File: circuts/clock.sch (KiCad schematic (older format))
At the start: 20 parts, among them P1 IN, P2 OUT, P3 LED OUTPUT, P4 PWR 12v, Q1 2N7002, Q2 2N7002, Q3 2N7002, Q4 2N7002, Q5 2N7002, Q6 2N7002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

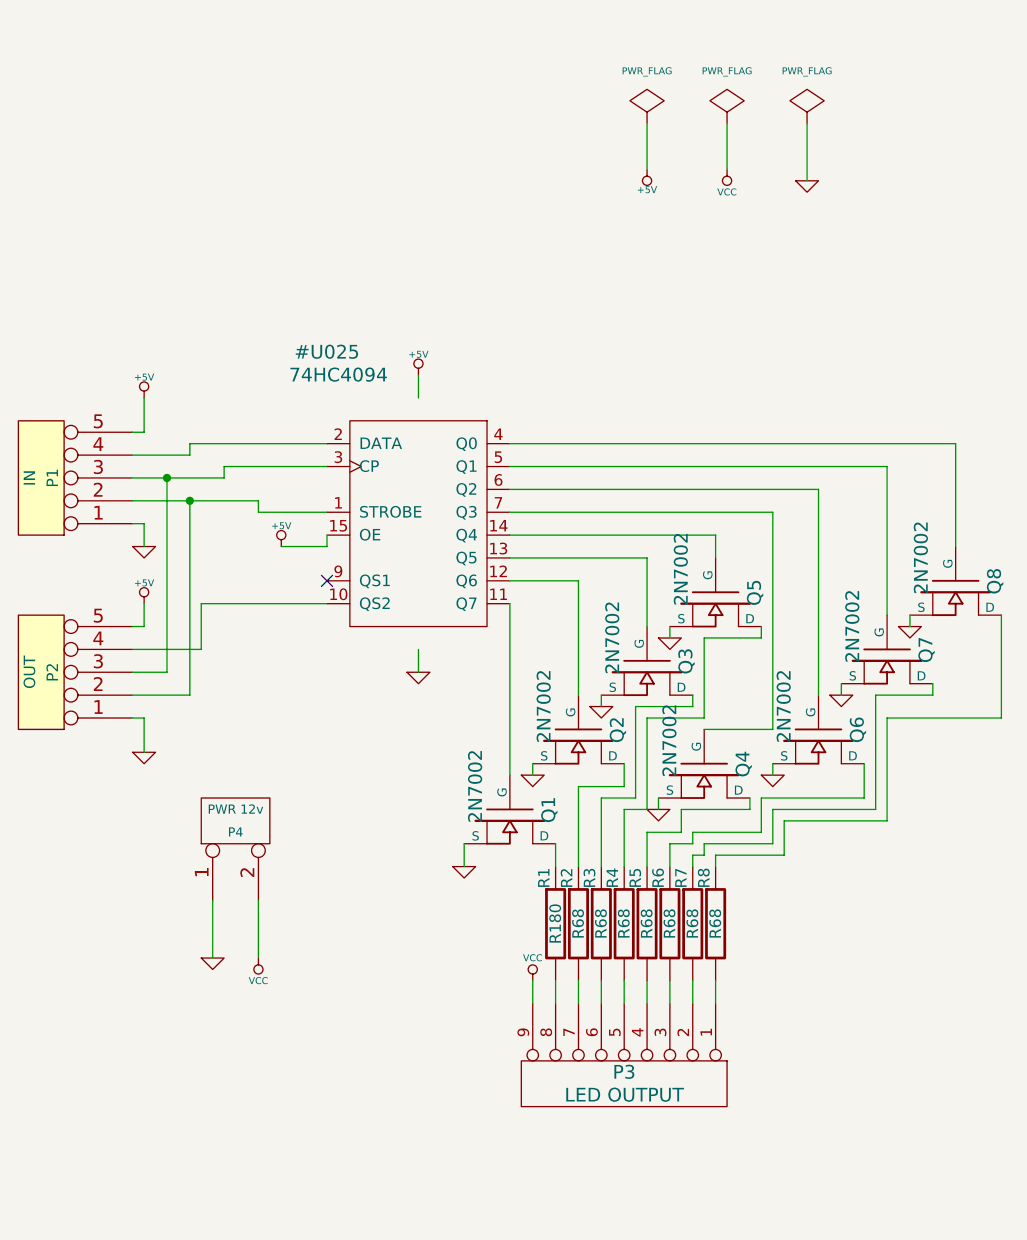
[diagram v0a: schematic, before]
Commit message: Release of circut for LED output
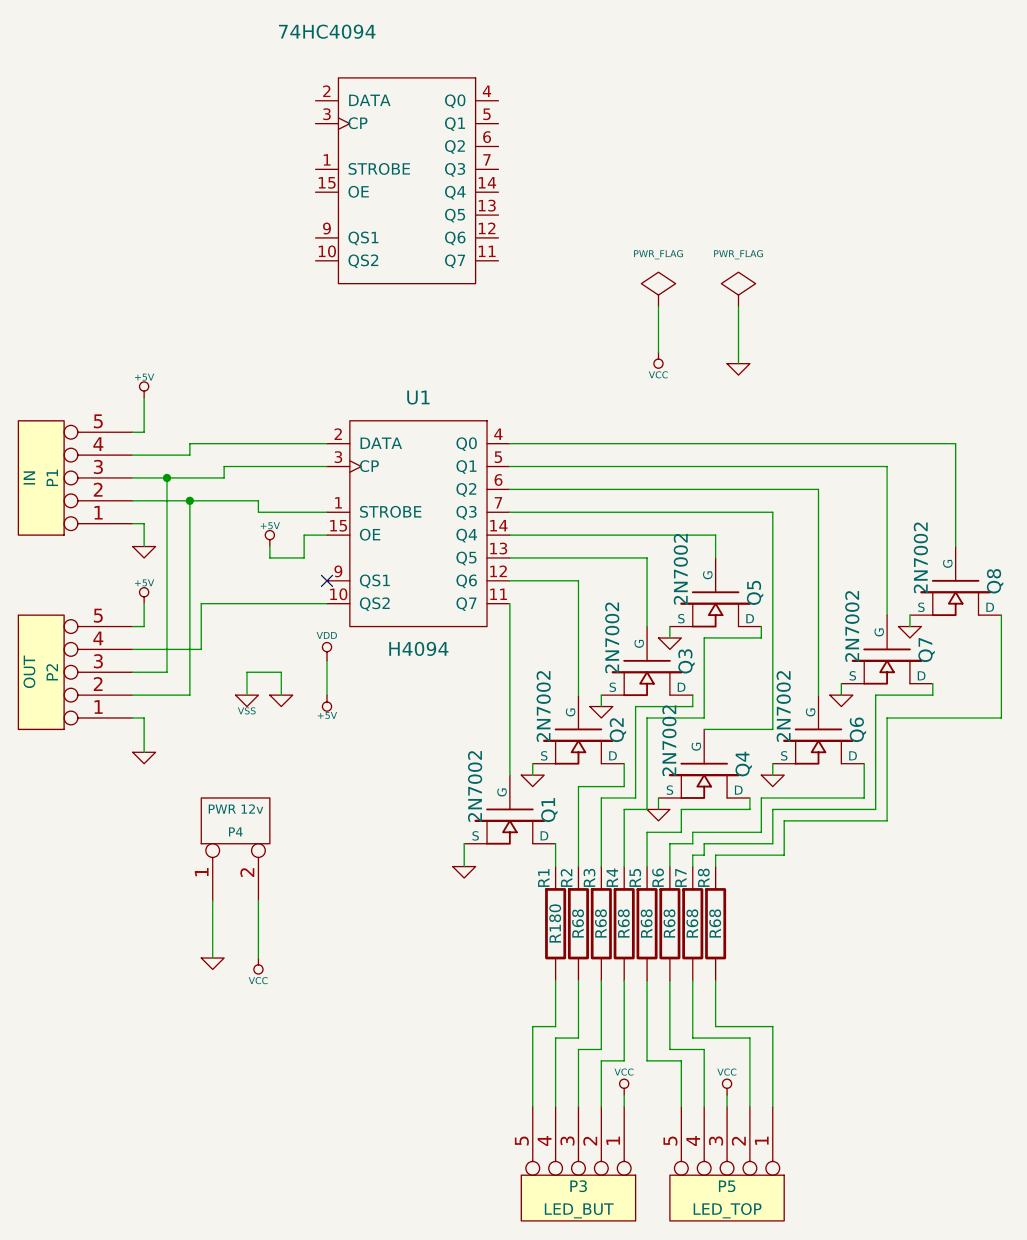
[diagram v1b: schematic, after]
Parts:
- removed P3: LED OUTPUT, symbol CONN_9
- added P3: LED_BUT, symbol CONN_5
- added P5: LED_TOP, symbol CONN_5
- added U1: H4094, symbol 22
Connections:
- net +5V: now also U1.15 (OE), U1.16 (VDD); no longer P4.2 (PM)
- net GND: now also U1.8 (VSS)
- net at P1.2, P2.2: now also U1.1 (STROBE)
- net at P1.3, P2.3: now also U1.3 (CP)
- net at P1.4: now also U1.2 (DATA)
- net at P2.4: now also U1.10 (QS2)
- net at R8.2: now also P5.1
- net at R7.2: now also P5.2
- net at R6.2: now also P5.4
- net at R5.2: now also P5.5
- net at R4.2: now also P3.2
- net at R3.2: now also P3.3
- net at R2.2: now also P3.4
- net at R1.2: now also P3.5
- net at Q1.G: now also U1.11 (Q7)
- net at Q2.G: now also U1.12 (Q6)
- net at Q3.G: now also U1.13 (Q5)
- net at Q5.G: now also U1.14 (Q4)
- net at Q4.G: now also U1.7 (Q3)
- net at Q6.G: now also U1.6 (Q2)
- net at Q7.G: now also U1.5 (Q1)
- net at Q8.G: now also U1.4 (Q0)
- new net VCC: P3.1, P4.2 (PM), P5.3
